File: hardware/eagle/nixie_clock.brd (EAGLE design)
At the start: 171.4 x 168.9 mm, 62 parts, among them IC1 74141N, IC10 7477N, IC11 74141N, IC12 7477N, IC13 74AC11238, IC2 7477N, IC3 74141N, IC4 7477N, IC5 74141N, IC6 7477N, IC7 74141N, IC8 7477N, IC9 74141N, J1_180V 22-27-2021-02, J1_5V1 22-27-2021-02, J1_5V2 22-27-2021-02

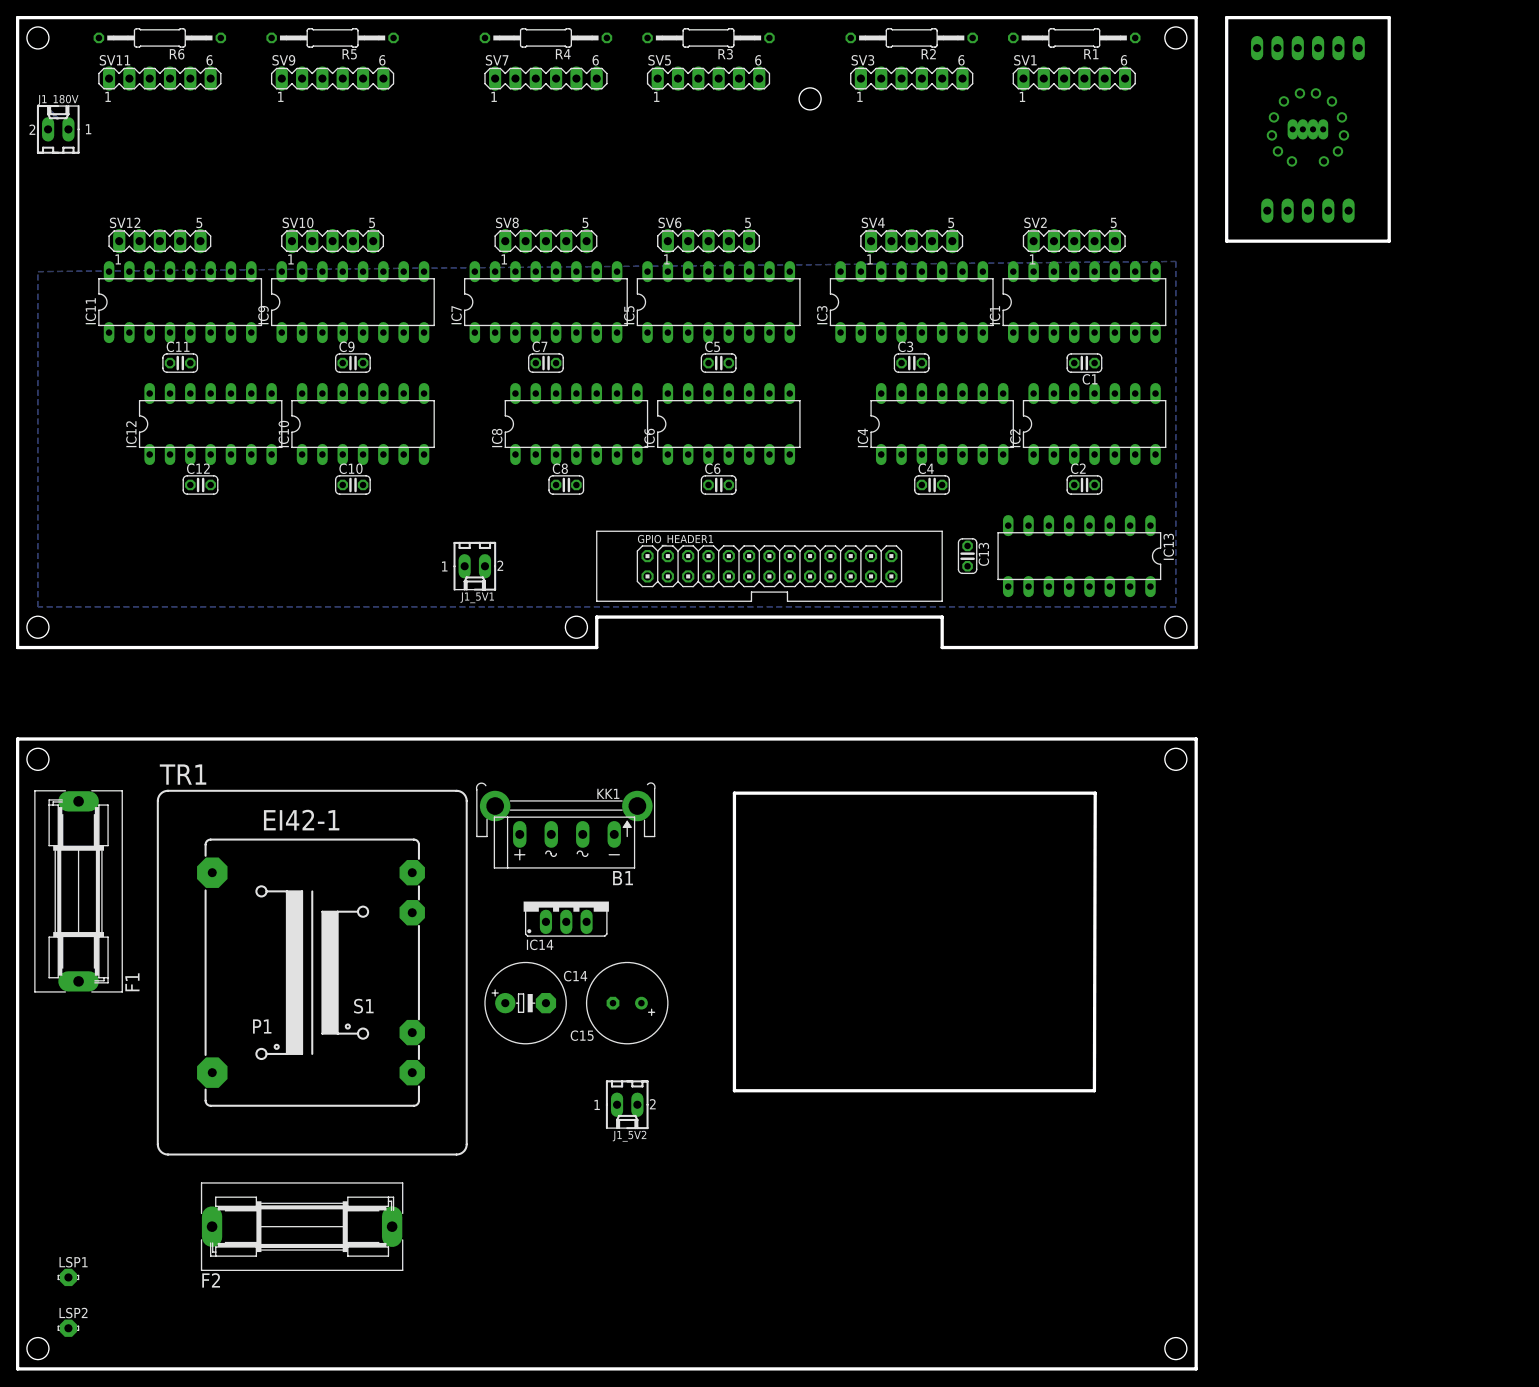
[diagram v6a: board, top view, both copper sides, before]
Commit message: Added relay
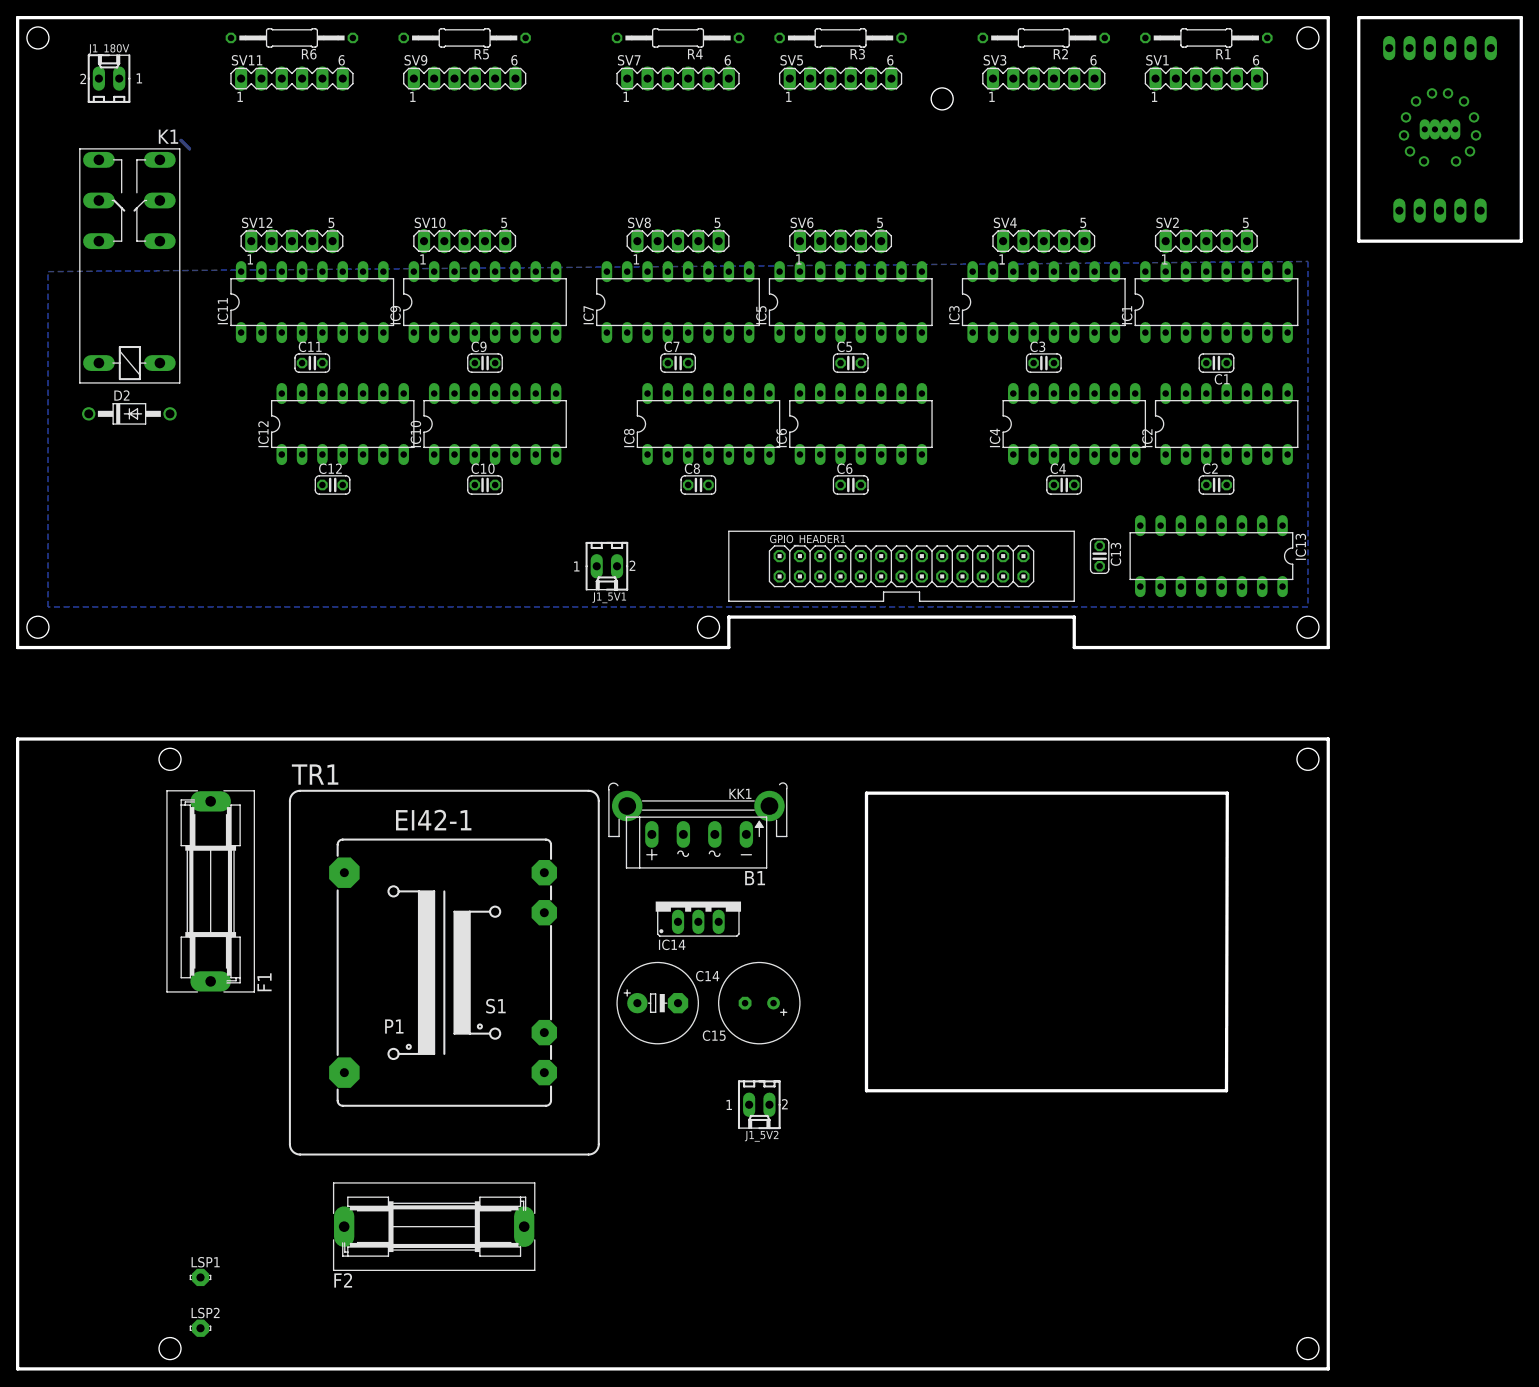
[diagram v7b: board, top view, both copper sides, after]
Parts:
- added D2: 1N4004, diode:DO41-10
- added K1: 4052, relay:F4052
- moved C1 16.5 mm to (149.9, 35.6)
- moved C2 16.5 mm to (149.9, 20.3)
- moved D1 16.5 mm to (177.8, 64.8)
- moved IC1 16.5 mm to (149.9, 43.2)
- moved IC4 16.5 mm to (132.1, 27.9)
- moved IN-8-1 16.5 mm to (177.8, 64.8)
- moved SV13 16.5 mm to (177.8, 74.9)
- moved SV14 16.5 mm to (177.8, 54.6)
- moved B1 16.5 mm to (85.1, -24.1)
- moved C10 16.5 mm to (58.4, 20.3)
- moved C14 16.5 mm to (80.0, -44.5)
- moved C3 16.5 mm to (128.3, 35.6)
- moved C4 16.5 mm to (130.8, 20.3)
- moved C5 16.5 mm to (104.1, 35.6)
- moved C6 16.5 mm to (104.1, 20.3)
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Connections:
- new net N$126: J1_180V.2, K1.P1, K1.P2
- new net N$129: D2.C, GPIO_HEADER1.7, K1.1
- net GND: now also D2.A, K1.2
- net VCC: now also K1.S1, K1.S2; no longer J1_180V.2
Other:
- board size 171.4 x 168.9 mm -> 188 x 168.9 mm

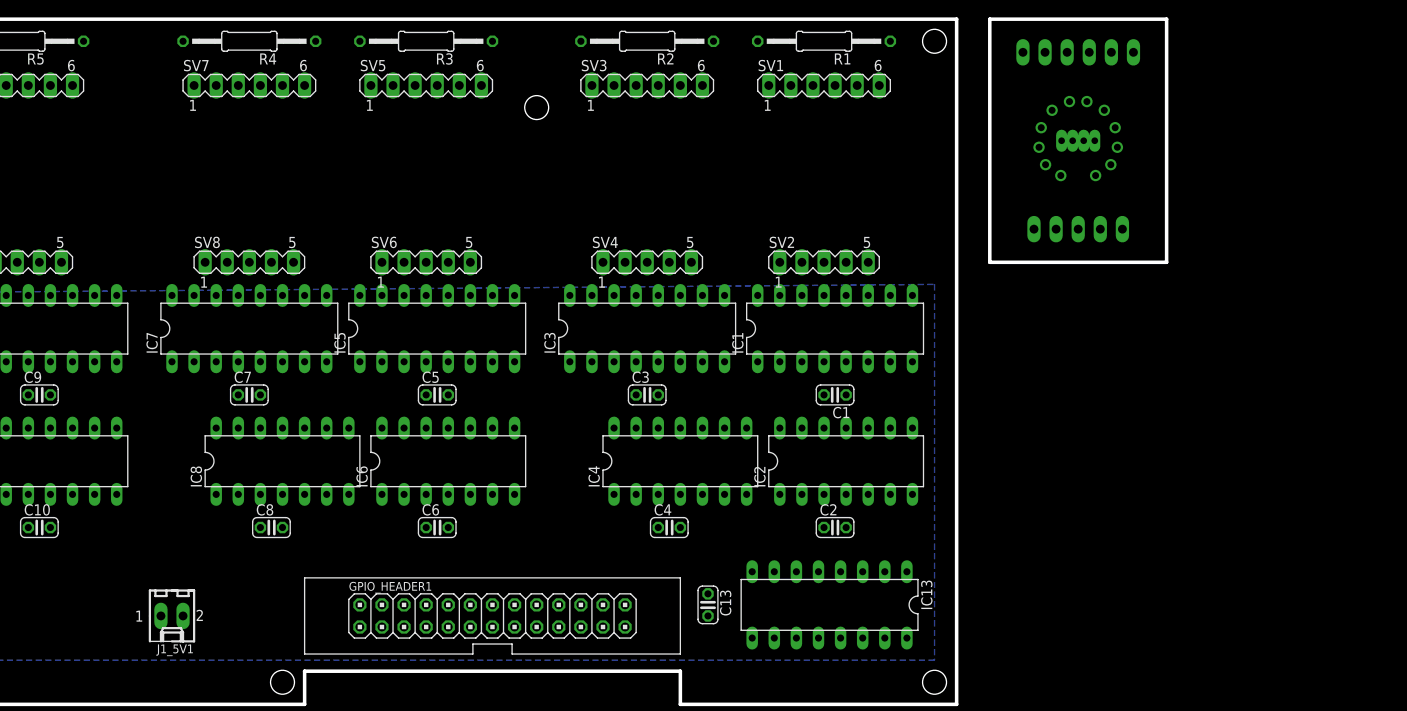
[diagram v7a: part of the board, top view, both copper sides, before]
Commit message: Added rotary encoder example
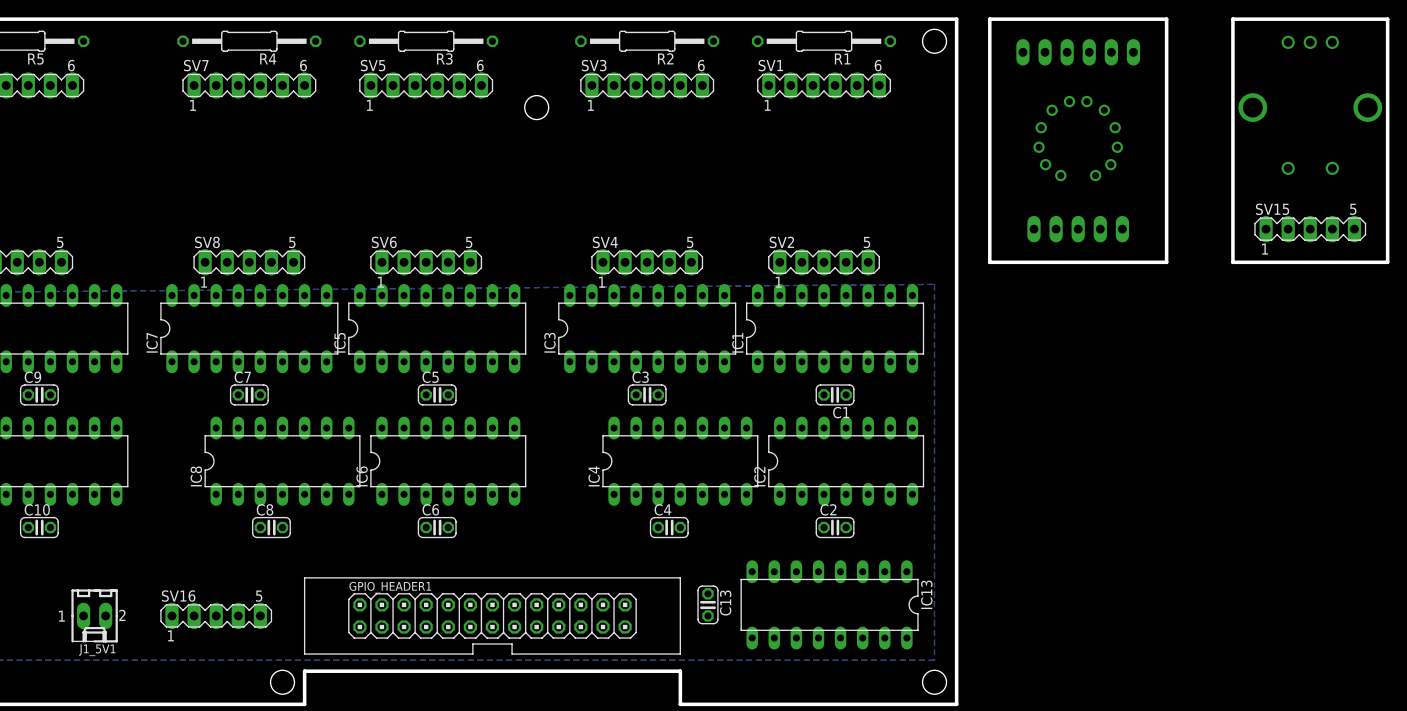
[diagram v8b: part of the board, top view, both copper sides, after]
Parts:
- removed D1: LED-RGB-CC-THRUCLEAR, SparkFun-LED:LED-RGB-THRU
- added SV15, SV16: (no value), con-lstb:MA05-1
- added SW1: ROTARTY_ENCODER, SparkFun-Electromechanical:ROTARY_ENC_PLAIN
- moved J1_5V1 8.89 mm to (64.8, 10.2)
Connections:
- new net N$127: GPIO_HEADER1.19, SV16.4
- new net N$128: SV15.4, SW1.A
- new net N$130: GPIO_HEADER1.24
- new net N$131: SV15.3, SW1.SW-
- new net N$132: SV15.1, SW1.SW+
- new net N$133: SV15.2, SW1.C
- new net N$134: SV15.5, SW1.B
- new net N$135: GPIO_HEADER1.26, SV16.5
- new net N$136: GPIO_HEADER1.21, SV16.3
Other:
- board size 188 x 168.9 mm -> 213.4 x 168.9 mm
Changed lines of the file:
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@@
 <wire x1="151.21" y1="-18.2" x2="106.11" y2="-18.2" width="0.4064" layer="20"/>
 <wire x1="106.11" y1="-18.2" x2="106.11" y2="-55.4" width="0.4064" layer="20"/>
+<wire x1="195.58" y1="78.74" x2="213.36" y2="78.74" width="0.4064" layer="20"/>
+<wire x1="213.36" y1="78.74" x2="213.36" y2="50.8" width="0.4064" layer="20"/>
+<wire x1="213.36" y1="50.8" x2="195.58" y2="50.8" width="0.4064" layer="20"/>
+<wire x1="195.58" y1="50.8" x2="195.58" y2="78.74" width="0.4064" layer="20"/>
 </plain>
 <attributes>
@@
 <attribute name="OC_FARNELL" value="unknown" x="11.43" y="71.12" size="1.778" layer="27" display="off"/>
 </element>
-<element name="J1_5V1" library="con-molex" package="6410-02" value="22-27-2021-02" x="73.66" y="10.16" rot="R180">
-<attribute name="OC_NEWARK" value="unknown" x="73.66" y="10.16" size="1.778" layer="27" rot="R180" display="off"/>
-<attribute name="MPN" value="" x="73.66" y="10.16" size="1.778" layer="27" rot="R180" display="off"/>
-<attribute name="MF" value="" x="73.66" y="10.16" size="1.778" layer="27" rot="R180" display="off"/>
-<attribute name="OC_FARNELL" value="unknown" x="73.66" y="10.16" size="1.778" layer="27" rot="R180" display="off"/>
+<element name="J1_5V1" library="con-molex" package="6410-02" value="22-27-2021-02" x="64.77" y="10.16" rot="R180">
+<attribute name="OC_NEWARK" value="unknown" x="64.77" y="10.16" size="1.778" layer="27" rot="R180" display="off"/>
+<attribute name="MPN" value="" x="64.77" y="10.16" size="1.778" layer="27" rot="R180" display="off"/>
+<attribute name="MF" value="" x="64.77" y="10.16" size="1.778" layer="27" rot="R180" display="off"/>
+<attribute name="OC_FARNELL" value="unknown" x="64.77" y="10.16" size="1.778" layer="27" rot="R180" display="off"/>
 </element>
 <element name="SV13" library="con-lstb" package="MA06-1" value="" x="177.8" y="74.93" rot="MR180">
@@
 <attribute name="OC_FARNELL" value="unknown" x="92.71" y="-57.15" size="1.778" layer="27" rot="R180" display="off"/>
 </element>
-<element name="D1" library="SparkFun-LED" package="LED-RGB-THRU" value="LED-RGB-CC-THRUCLEAR" x="177.8" y="64.77" rot="MR0">
-<attribute name="PROD_ID" value="DIO-08418" x="177.8" y="64.77" size="1.778" layer="28" rot="MR0" display="off"/>
-</element>
 <element name="K1" library="relay" package="F4052" value="4052" x="13.97" y="39.37" rot="R90"/>
 <element name="D2" library="diode" package="DO41-10" value="1N4004" x="13.97" y="29.21"/>
+<element name="SW1" library="SparkFun-Electromechanical" package="ROTARY_ENC_PLAIN" value="ROTARTY_ENCODER" x="204.47" y="68.58" rot="MR90"/>
+<element name="SV15" library="con-lstb" package="MA05-1" value="" x="204.47" y="54.61">
+<attribute name="OC_NEWARK" value="unknown" x="204.47" y="54.61" size="1.778" layer="27" display="off"/>
+<attribute name="MPN" value="" x="204.47" y="54.61" size="1.778" layer="27" display="off"/>
+<attribute name="MF" value="" x="204.47" y="54.61" size="1.778" layer="27" display="off"/>
+<attribute name="OC_FARNELL" value="unknown" x="204.47" y="54.61" size="1.778" layer="27" display="off"/>
+</element>
+<element name="SV16" library="con-lstb" package="MA05-1" value="" x="78.74" y="10.16">
+<attribute name="OC_NEWARK" value="unknown" x="78.74" y="10.16" size="1.778" layer="27" display="off"/>
+<attribute name="MPN" value="" x="78.74" y="10.16" size="1.778" layer="27" display="off"/>
+<attribute name="MF" value="" x="78.74" y="10.16" size="1.778" layer="27" display="off"/>
+<attribute name="OC_FARNELL" value="unknown" x="78.74" y="10.16" size="1.778" layer="27" display="off"/>
+</element>
 </elements>
 <signals>
@@
 <wire x1="83.82" y1="46.99" x2="81.28" y2="35.56" width="0" layer="19" extent="1-1"/>
 <wire x1="83.82" y1="20.32" x2="86.36" y2="31.75" width="0" layer="19" extent="1-1"/>
-<wire x1="72.39" y1="10.16" x2="83.82" y2="20.32" width="0" layer="19" extent="1-1"/>
-<wire x1="57.15" y1="20.32" x2="72.39" y2="10.16" width="0" layer="19" extent="1-1"/>
+<wire x1="63.5" y1="10.16" x2="83.82" y2="20.32" width="0" layer="19" extent="1-1"/>
+<wire x1="57.15" y1="20.32" x2="63.5" y2="10.16" width="0" layer="19" extent="1-1"/>
 <wire x1="59.69" y1="31.75" x2="57.15" y2="20.32" width="0" layer="19" extent="1-1"/>
 <wire x1="57.15" y1="35.56" x2="59.69" y2="31.75" width="0" layer="19" extent="1-1"/>
@@
 <wire x1="19.05" y1="29.21" x2="35.56" y2="35.56" width="0" layer="19" extent="1-1"/>
 <wire x1="17.78" y1="35.56" x2="19.05" y2="29.21" width="0" layer="19" extent="1-1"/>
-<wire x1="12.7" y1="71.12" x2="17.78" y2="35.56" width="0" layer="19" extent="1-1"/>
+<wire x1="12.7" y1="71.12" x2="38.1" y2="46.99" width="0" layer="19" extent="1-1"/>
 </signal>
 <signal name="+5V">
@@
 <wire x1="83.82" y1="35.56" x2="86.36" y2="24.13" width="0" layer="19" extent="1-1"/>
 <wire x1="83.82" y1="39.37" x2="83.82" y2="35.56" width="0" layer="19" extent="1-1"/>
-<wire x1="74.93" y1="10.16" x2="86.36" y2="20.32" width="0" layer="19" extent="1-1"/>
-<wire x1="59.69" y1="20.32" x2="74.93" y2="10.16" width="0" layer="19" extent="1-1"/>
+<wire x1="66.04" y1="10.16" x2="86.36" y2="20.32" width="0" layer="19" extent="1-1"/>
+<wire x1="59.69" y1="20.32" x2="66.04" y2="10.16" width="0" layer="19" extent="1-1"/>
 <wire x1="59.69" y1="24.13" x2="59.69" y2="20.32" width="0" layer="19" extent="1-1"/>
 <wire x1="59.69" y1="35.56" x2="59.69" y2="24.13" width="0" layer="19" extent="1-1"/>
@@
 <wire x1="10.16" y1="35.56" x2="8.89" y2="29.21" width="0" layer="19" extent="1-1"/>
 </signal>
+<signal name="N$127">
+<contactref element="SV16" pad="4"/>
+<contactref element="GPIO_HEADER1" pad="19"/>
+<wire x1="118.11" y1="8.89" x2="81.28" y2="10.16" width="0" layer="19" extent="1-1"/>
+</signal>
+<signal name="N$130">
+<contactref element="GPIO_HEADER1" pad="24"/>
+</signal>
+<signal name="N$131">
+<contactref element="SW1" pad="SW-"/>
+<contactref element="SV15" pad="3"/>
+<wire x1="201.93" y1="61.595" x2="204.47" y2="54.61" width="0" layer="19" extent="1-1"/>
+</signal>
+<signal name="N$132">
+<contactref element="SV15" pad="1"/>
+<contactref element="SW1" pad="SW+"/>
+<wire x1="207.01" y1="61.595" x2="199.39" y2="54.61" width="0" layer="19" extent="1-1"/>
+</signal>
+<signal name="N$133">
+<contactref element="SW1" pad="C"/>
+<contactref element="SV15" pad="2"/>
+<wire x1="204.47" y1="76.073" x2="201.93" y2="54.61" width="0" layer="19" extent="1-1"/>
+</signal>
+<signal name="N$135">
+<contactref element="SV16" pad="5"/>
+<contactref element="GPIO_HEADER1" pad="26"/>
+<wire x1="83.82" y1="10.16" x2="125.73" y2="11.43" width="0" layer="19" extent="1-1"/>
+</signal>
+<signal name="N$136">
+<contactref element="SV16" pad="3"/>
+<contactref element="GPIO_HEADER1" pad="21"/>
+<wire x1="120.65" y1="8.89" x2="78.74" y2="10.16" width="0" layer="19" extent="1-1"/>
+</signal>
+<signal name="N$128">
+<contactref element="SW1" pad="A"/>
+<contactref element="SV15" pad="4"/>
+<wire x1="201.93" y1="76.073" x2="207.01" y2="54.61" width="0" layer="19" extent="1-1"/>
+</signal>
+<signal name="N$134">
+<contactref element="SW1" pad="B"/>
+<contactref element="SV15" pad="5"/>
+<wire x1="207.01" y1="76.073" x2="209.55" y2="54.61" width="0" layer="19" extent="1-1"/>
+</signal>
 </signals>
